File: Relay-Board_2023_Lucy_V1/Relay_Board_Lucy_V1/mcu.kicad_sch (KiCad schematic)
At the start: 30 parts, among them J6 DE9_Receptacle_MountingHoles, J7 USB_B_Micro, J8 SWD_HEADER, SW3 Hard Reset Button, SW4 Boot Button, U10 STM32F722RETx, U7 MCP2542FD, X1 OXETDLJANF-8MHZ

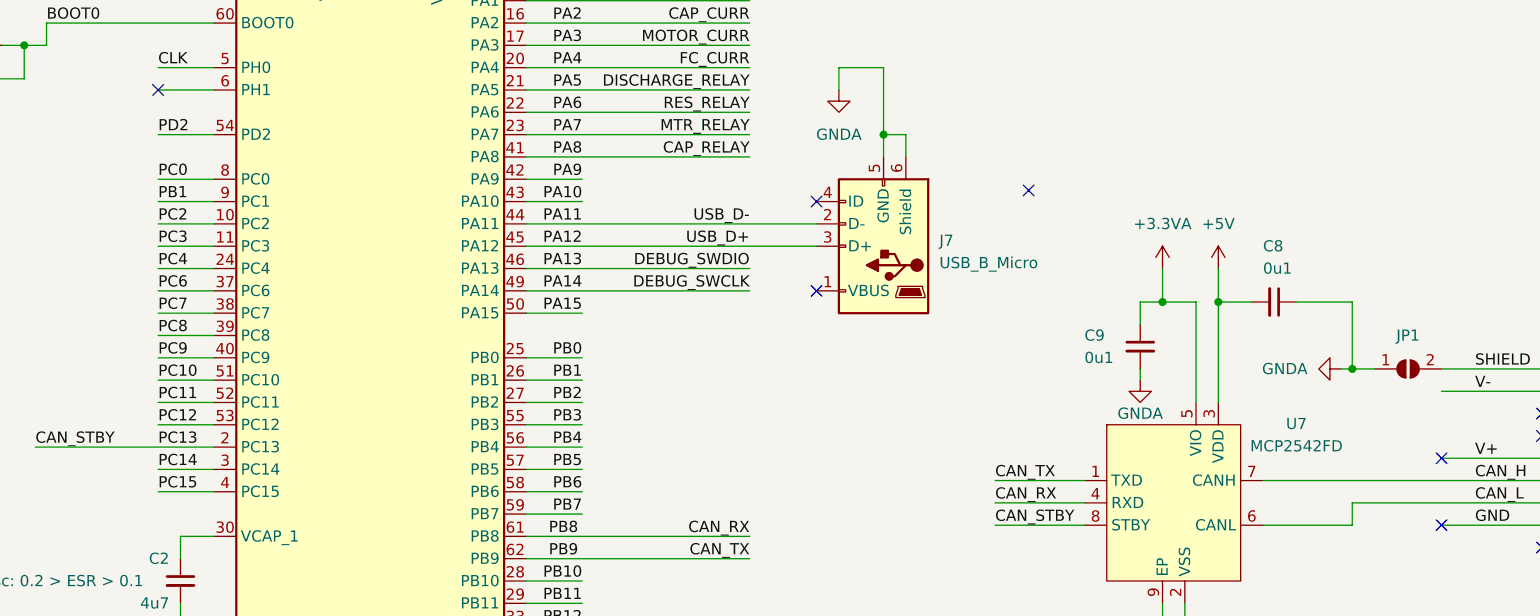
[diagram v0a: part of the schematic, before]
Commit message: Big changes to relay board
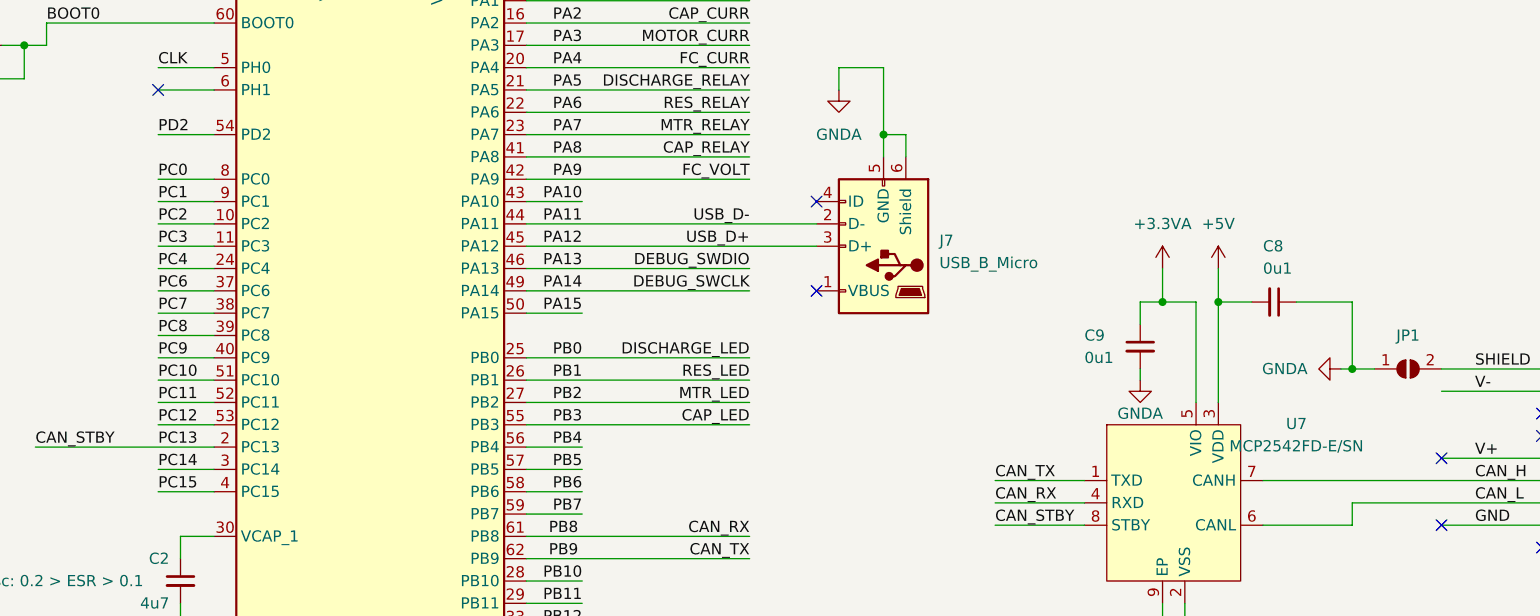
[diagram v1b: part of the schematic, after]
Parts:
- U7: value MCP2542FD -> MCP2542FD-E/SN; footprint Package_DFN_QFN:DFN-8-1EP_3x3mm_P0.65mm_EP1.55x2.4mm -> Package_SO:SOIC-8_3.9x4.9mm_P1.27mm
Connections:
- net PB1: no longer U10.9 (PC1)
- net PA9 renamed FC_VOLT
- net PB0 renamed DISCHARGE_LED
- net PB2 renamed MTR_LED
- net PB3 renamed CAP_LED
- new net PC1: U10.9 (PC1)
- no-connect marks 11 -> 10
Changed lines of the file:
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@@
   (no_connect (at 227.33 133.35))
   (no_connect (at 64.77 27.94))
-  (no_connect (at 180.34 102.87))
   (no_connect (at 81.28 91.44))
   (no_connect (at 238.76 128.27))
@@
     (stroke (width 0) (type default))
   )
-  (wire (pts (xy 123.19 101.6) (xy 129.54 101.6))
+  (wire (pts (xy 123.19 101.6) (xy 148.59 101.6))
     (stroke (width 0) (type default))
   )
@@
     (stroke (width 0) (type default))
   )
-  (wire (pts (xy 123.19 129.54) (xy 129.54 129.54))
+  (wire (pts (xy 123.19 129.54) (xy 148.59 129.54))
     (stroke (width 0) (type default))
   )
@@
     (stroke (width 0) (type default))
   )
-  (wire (pts (xy 123.19 121.92) (xy 129.54 121.92))
+  (wire (pts (xy 123.19 121.92) (xy 148.59 121.92))
     (stroke (width 0) (type default))
   )
@@
     (stroke (width 0) (type default))
   )
-  (wire (pts (xy 123.19 124.46) (xy 129.54 124.46))
+  (wire (pts (xy 123.19 124.46) (xy 148.59 124.46))
     (stroke (width 0) (type default))
   )
@@
     (stroke (width 0) (type default))
   )
-  (wire (pts (xy 123.19 127) (xy 129.54 127))
+  (wire (pts (xy 123.19 127) (xy 148.59 127))
     (stroke (width 0) (type default))
   )
@@
     (effects (font (size 1.27 1.27)) (justify right bottom))
   )
+  (label "RES_LED" (at 148.59 124.46 180) (fields_autoplaced)
+    (effects (font (size 1.27 1.27)) (justify right bottom))
+  )
+  (label "MTR_LED" (at 148.59 127 180) (fields_autoplaced)
+    (effects (font (size 1.27 1.27)) (justify right bottom))
+  )
   (label "PA13" (at 129.54 111.76 180) (fields_autoplaced)
     (effects (font (size 1.27 1.27)) (justify right bottom))
@@
     (effects (font (size 1.27 1.27)) (justify left bottom))
   )
+  (label "DISCHARGE_LED" (at 148.59 121.92 180) (fields_autoplaced)
+    (effects (font (size 1.27 1.27)) (justify right bottom))
+  )
   (label "CAN_TX" (at 176.53 135.89 0) (fields_autoplaced)
     (effects (font (size 1.27 1.27)) (justify left bottom))
@@
     (effects (font (size 1.27 1.27)) (justify left bottom))
   )
-  (label "PB1" (at 81.28 104.14 0) (fields_autoplaced)
+  (label "PC1" (at 81.28 104.14 0) (fields_autoplaced)
     (effects (font (size 1.27 1.27)) (justify left bottom))
   )
@@
     (effects (font (size 1.27 1.27)) (justify left bottom))
   )
+  (label "CAP_LED" (at 148.59 129.54 180) (fields_autoplaced)
+    (effects (font (size 1.27 1.27)) (justify right bottom))
+  )
   (label "PB3" (at 129.54 129.54 180) (fields_autoplaced)
     (effects (font (size 1.27 1.27)) (justify right bottom))
@@
   )
   (label "PA9" (at 129.54 101.6 180) (fields_autoplaced)
+    (effects (font (size 1.27 1.27)) (justify right bottom))
+  )
+  (label "FC_VOLT" (at 148.59 101.6 180) (fields_autoplaced)
     (effects (font (size 1.27 1.27)) (justify right bottom))
   )
@@
       (effects (font (size 1.27 1.27)))
     )
-    (property "Value" "MCP2542FD" (at 210.82 131.9783 0)
+    (property "Value" "MCP2542FD-E/SN" (at 210.82 131.9783 0)
       (effects (font (size 1.27 1.27)))
     )
-    (property "Footprint" "Package_DFN_QFN:DFN-8-1EP_3x3mm_P0.65mm_EP1.55x2.4mm" (at 165.1 121.92 0)
-      (effects (font (size 1.27 1.27)) hide)
-    )
-    (property "Datasheet" "" (at 165.1 121.92 0)
-      (effects (font (size 1.27 1.27)) hide)
-    )
+    (property "Footprint" "Package_SO:SOIC-8_3.9x4.9mm_P1.27mm" (at 165.1 121.92 0)
+      (effects (font (size 1.27 1.27)) hide)
+    )
+    (property "Datasheet" "https://ww1.microchip.com/downloads/aemDocuments/documents/APID/ProductDocuments/DataSheets/MCP2542FD-MCP2542WFD-4WFD-Data-Sheet-DS20005514C.pdf" (at 165.1 121.92 0)
+      (effects (font (size 1.27 1.27)) hide)
+    )

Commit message: added a socket
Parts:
- added J4: Conn_02x14_Top_Bottom, Connector_PinSocket_1.27mm:PinSocket_2x14_P1.27mm_Vertical, symbol Connector_Generic:Conn_02x14_Odd_Even
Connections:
- net PA10: now also J4.2 (Pin_2)
- net PA15: now also J4.4 (Pin_4)
- net PB10: now also J4.14 (Pin_14)
- net PB11: now also J4.16 (Pin_16)
- net PB12: now also J4.18 (Pin_18)
- net PB13: now also J4.20 (Pin_20)
- net PB14: now also J4.22 (Pin_22)
- net PB15: now also J4.24 (Pin_24)
- net PB4: now also J4.6 (Pin_6)
- net PB5: now also J4.8 (Pin_8)
- net PB6: now also J4.10 (Pin_10)
- net PB7: now also J4.12 (Pin_12)
- net PC0: now also J4.1 (Pin_1)
- net PC1: now also J4.3 (Pin_3)
- net PC10: now also J4.19 (Pin_19)
- net PC11: now also J4.21 (Pin_21)
- net PC12: now also J4.23 (Pin_23)
- net PC14: now also J4.25 (Pin_25)
- net PC15: now also J4.27 (Pin_27)
- net PC2: now also J4.5 (Pin_5)
- net PC3: now also J4.7 (Pin_7)
- net PC4: now also J4.9 (Pin_9)
- net PC6: now also J4.11 (Pin_11)
- net PC7: now also J4.13 (Pin_13)
- net PC8: now also J4.15 (Pin_15)
- net PC9: now also J4.17 (Pin_17)
- net PD2: now also J4.26 (Pin_26)
- no-connect marks 10 -> 11

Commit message: Updates
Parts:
- removed JP2: Jumper_2_Bridged, symbol Jumper:Jumper_2_Bridged
- removed JP3: Jumper_2_Open, symbol Jumper:Jumper_2_Open
- removed U10: STM32F722RETx, Package_QFP:LQFP-64_10x10mm_P0.5mm, symbol MCU_ST_STM32F7:STM32F722RETx
- added C20: 100n, Capacitor_SMD:C_0603_1608Metric, symbol Device:C_Small
- added JP1: SolderJumper_2_Open, Jumper:SolderJumper-2_P1.3mm_Open_TrianglePad1.0x1.5mm, symbol Jumper:SolderJumper_2_Open
- added JP2: SolderJumper_2_Bridged, Jumper:SolderJumper-2_P1.3mm_Bridged_RoundedPad1.0x1.5mm, symbol Jumper:SolderJumper_2_Bridged
- added U10: STM32F446RETx, Package_QFP:LQFP-64_10x10mm_P0.5mm, symbol MCU_ST_STM32F4:STM32F446RETx
- C10: renamed from C11; footprint (none) -> Capacitor_SMD:C_0603_1608Metric
- C11: renamed from C31; footprint (none) -> Capacitor_SMD:C_0603_1608Metric
- C12: renamed from C16; footprint (none) -> Capacitor_SMD:C_0603_1608Metric
- C13: renamed from C24; footprint (none) -> Capacitor_SMD:C_0603_1608Metric
- C14: renamed from C12; footprint (none) -> Capacitor_SMD:C_0603_1608Metric
- C15: renamed from C25; footprint (none) -> Capacitor_SMD:C_0603_1608Metric
- C16: renamed from C13; footprint (none) -> Capacitor_SMD:C_0603_1608Metric
- C17: renamed from C29; footprint (none) -> Capacitor_SMD:C_0603_1608Metric
- C18: renamed from C2; footprint (none) -> Capacitor_SMD:C_0603_1608Metric
- C19: renamed from C30; footprint (none) -> Capacitor_SMD:C_0603_1608Metric
- C21: renamed from C26; footprint (none) -> Capacitor_SMD:C_0603_1608Metric
- C22: renamed from C27; footprint (none) -> Capacitor_SMD:C_0603_1608Metric
- C23: renamed from C9; value 0u1 -> 100n; footprint (none) -> Capacitor_SMD:C_0603_1608Metric
- C24: renamed from C8; value 0u1 -> 100n; footprint (none) -> Capacitor_SMD:C_0603_1608Metric
- C8: renamed from C10; footprint (none) -> Capacitor_SMD:C_0603_1608Metric
- C9: renamed from C1; footprint (none) -> Capacitor_SMD:C_0603_1608Metric
- FB1: renamed from FB2; footprint (none) -> Inductor_SMD:L_1206_3216Metric
- J6: renamed from J8; footprint (none) -> Connector_PinSocket_2.54mm:PinSocket_1x04_P2.54mm_Vertical
- J7: footprint (none) -> Connector_Dsub:DSUB-9_Female_Horizontal_P2.77x2.84mm_EdgePinOffset7.70mm_Housed_MountingHolesOffset9.12mm
- J9: renamed from J6; footprint (none) -> Connector_Dsub:DSUB-9_Female_Horizontal_P2.77x2.84mm_EdgePinOffset7.70mm_Housed_MountingHolesOffset9.12mm
- JP3: renamed from JP1; footprint (none) -> Jumper:SolderJumper-2_P1.3mm_Open_TrianglePad1.0x1.5mm
- R25: renamed from R10; footprint (none) -> Resistor_SMD:R_0603_1608Metric
- SW1: renamed from SW3; value Hard Reset Button -> PTS815 SJM 250 SMTR LFS; footprint (none) -> Button_Switch_SMD:SW_SPST_PTS810
- SW2: renamed from SW4; value Boot Button -> PTS815 SJM 250 SMTR LFS; footprint (none) -> Inductor_SMD:L_1206_3216Metric
- U7: renamed from U5; value ~ -> LD39050PU33R; footprint (none) -> Package_DFN_QFN:DFN-6-1EP_3x3mm_P0.95mm_EP1.7x2.6mm
- renumbered J4 to J8, U7 to U9
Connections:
- net PC12 is gone; now on net PC13: J8.23 (Pin_23)
- net +3.3VA: now also U10.13 (VDDA)
- net +3V3: now also C20.1, JP2.1 (A), U10.1 (VBAT), U10.19 (VDD), U10.32 (VDD), U10.48 (VDD), U10.64 (VDD)
- net +5V: now also JP1.1 (A)
- net BOOT0: now also U10.60 (BOOT0)
- net CAN_RX: now also U10.61 (PB8)
- net CAN_STBY: now also U10.53 (PC12)
- net CAN_TX: now also U10.62 (PB9)
- net CAP_CURR: now also U10.16 (PA2)
- net CAP_LED: now also U10.55 (PB3)
- net CAP_RELAY: now also U10.41 (PA8)
- net CAP_VOLT: now also U10.15 (PA1)
- net CLK: now also U10.5 (PH0)
- net DEBUG_SWCLK: now also U10.49 (PA14)
- net DEBUG_SWDIO: now also U10.46 (PA13)
- net DISCHARGE_LED: now also U10.26 (PB0)
- net DISCHARGE_RELAY: now also U10.21 (PA5)
- net FC_CURR: now also U10.20 (PA4)
- net FC_VOLT: now also U10.42 (PA9)
- net GNDA: now also C20.2, U10.12 (VSSA), U10.18 (VSS), U10.31 (VSS), U10.47 (VSS), U10.63 (VSS)
- net MOTOR_CURR: now also U10.17 (PA3)
- net MTR_LED: now also U10.28 (PB2)
- net MTR_RELAY: now also U10.23 (PA7)
- net MTR_VOLT: now also U10.14 (PA0)
- net PA10: now also U10.43 (PA10)
- net PA11: now also U10.44 (PA11)
- net PA12: now also U10.45 (PA12)
- net PA15: now also U10.50 (PA15)
- net PA6: now also U10.22 (PA6)
- net PB1: now also U10.27 (PB1)
- net PB10: now also U10.29 (PB10)
- net PB12: now also U10.33 (PB12)
- net PB13: now also U10.34 (PB13)
- net PB14: now also U10.35 (PB14)
- net PB15: now also U10.36 (PB15)
- net PB4: now also U10.56 (PB4)
- net PB5: now also U10.57 (PB5)
- net PB6: now also U10.58 (PB6)
- net PB7: now also U10.59 (PB7)
- net PC0: now also U10.8 (PC0)
- net PC1: now also U10.9 (PC1)
- net PC10: now also U10.51 (PC10)
- net PC11: now also U10.52 (PC11)
- net PC14: now also U10.3 (PC14)
- net PC15: now also U10.4 (PC15)
- net PC2: now also U10.10 (PC2)
- net PC3: now also U10.11 (PC3)
- net PC4: now also U10.24 (PC4)
- net PC6: now also U10.37 (PC6)
- net PC7: now also U10.38 (PC7)
- net PC8: now also U10.39 (PC8)
- net PC9: now also U10.40 (PC9)
- net PD2: now also U10.54 (PD2)
- net ~{RST}: now also U10.7 (NRST)
- net at J6.1 (Pin_1): now also JP1.2 (B), JP2.2 (B)
- net at C18.1: now also U10.30 (VCAP_1)
- net PC5: now reaches J8.28 (Pin_28)
- net PC5: now also U10.25 (PC5)
- net PB11 renamed PC13
- net PC13: now also U10.2 (PC13)
- no-connect marks 11 -> 10
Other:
- moved on the sheet: C12, C13, C15, C17, C18, C19

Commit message: Started the PCB design work
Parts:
- added TP1, TP2: TestPoint_Alt, TestPoint:TestPoint_THTPad_D2.0mm_Drill1.0mm, symbol Connector:TestPoint_Alt
- J7: footprint Connector_Dsub:DSUB-9_Female_Horizontal_P2.77x2.84mm_EdgePinOffset7.70mm_Housed_MountingHolesOffset9.12mm -> Connector_USB:USB_Micro-B_Wuerth_629105150521
- J8: footprint Connector_PinSocket_1.27mm:PinSocket_2x14_P1.27mm_Vertical -> Connector_PinSocket_2.54mm:PinSocket_2x14_P2.54mm_Vertical
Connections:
- net PA6 is gone; now on net CAP_VOLT: U10.22 (PA6)
- net CAN_STBY: now also U10.59 (PB7); no longer U10.53 (PC12)
- net CAP_CURR: now also U10.23 (PA7); no longer U10.16 (PA2)
- net CAP_LED: now also U10.36 (PB15); no longer U10.55 (PB3)
- net CAP_RELAY: now also U10.28 (PB2); no longer U10.41 (PA8)
- net CAP_VOLT: no longer U10.15 (PA1)
- net DISCHARGE_LED: now also U10.33 (PB12); no longer U10.26 (PB0)
- net DISCHARGE_RELAY: now also U10.26 (PB0); no longer U10.21 (PA5)
- net FC_CURR: now also U10.25 (PC5); no longer U10.20 (PA4)
- net FC_VOLT: now also U10.24 (PC4); no longer U10.42 (PA9)
- net GNDA: now also U7.7 (GND); no longer U7.0 (GND), U9.9 (EP)
- net MOTOR_CURR: now also U10.21 (PA5); no longer U10.17 (PA3)
- net MTR_LED: now also U10.35 (PB14); no longer U10.28 (PB2)
- net MTR_RELAY: now also U10.29 (PB10); no longer U10.23 (PA7)
- net MTR_VOLT: now also U10.20 (PA4); no longer U10.14 (PA0)
- net PA10: now also J8.22 (Pin_22); no longer J8.2 (Pin_2)
- net PA15: now also J8.18 (Pin_18); no longer J8.4 (Pin_4)
- net PB13: no longer J8.20 (Pin_20)
- net PB4: now also J8.4 (Pin_4); no longer J8.6 (Pin_6)
- net PB5: now also J8.6 (Pin_6); no longer J8.8 (Pin_8)
- net PB6: now also J8.8 (Pin_8); no longer J8.10 (Pin_10)
- net PC10: now also J8.10 (Pin_10); no longer J8.19 (Pin_19)
- net PC11: now also J8.12 (Pin_12); no longer J8.21 (Pin_21)
- net PC13: now also J8.17 (Pin_17); no longer J8.16 (Pin_16), J8.23 (Pin_23)
- net PC14: now also J8.19 (Pin_19); no longer J8.25 (Pin_25)
- net PC15: now also J8.21 (Pin_21); no longer J8.27 (Pin_27)
- net PC6: now also J8.23 (Pin_23); no longer J8.11 (Pin_11)
- net PC7: now also J8.25 (Pin_25); no longer J8.13 (Pin_13)
- net PC8: now also J8.27 (Pin_27); no longer J8.15 (Pin_15)
- net PC9: now also TP2.1; no longer J8.17 (Pin_17)
- net PD2: now also J8.16 (Pin_16); no longer J8.26 (Pin_26)
- net PB10 renamed PC12
- net PC12: now also U10.53 (PC12); no longer U10.29 (PB10)
- removed net PB12: J8.18 (Pin_18), U10.33 (PB12)
- removed net PB14: J8.22 (Pin_22), U10.35 (PB14)
- net PB15: no longer names the net of J8.24 (Pin_24)
- net PB15: no longer U10.36 (PB15)
- removed net PB7: J8.12 (Pin_12), U10.59 (PB7)
- net PC4 renamed PA0
- net PA0: now also U10.14 (PA0); no longer U10.24 (PC4)
- net PC5: no longer names the net of J8.28 (Pin_28)
- net PC5: no longer U10.25 (PC5)
- new net PA1: J8.11 (Pin_11), U10.15 (PA1)
- new net PA2: J8.13 (Pin_13), U10.16 (PA2)
- new net PA3: J8.15 (Pin_15), U10.17 (PA3)
- new net PA8: TP1.1, U10.41 (PA8)
- new net PA9: J8.20 (Pin_20), U10.42 (PA9)
- new net PB3: J8.2 (Pin_2), U10.55 (PB3)
- no-connect marks 10 -> 13
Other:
- moved on the sheet: J7
